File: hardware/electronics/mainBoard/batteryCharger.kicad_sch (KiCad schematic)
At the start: 48 parts, among them J11 M8AS-02PFFR-SF8001, J8 S2B-PH-SM4-TB, Q1 CSD17575Q3, Q6 VAL, Q7 VAL, Q8 VAL, Q9 VAL, U11 BQ25798

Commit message: added jumpers
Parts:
- added JP1: ~, symbol .DS-Jumpers:Jumper_2_Bridged
- R60: value 6K04 -> 8K2; DKPN 541-6.04KLCT-ND -> (none); MPN CRCW04026K04FKED -> (none)
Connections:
- net at D11.2: now also JP1.1; no longer U11.1 (STAT)
- new net: JP1.2, U11.1 (STAT)
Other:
- moved on the sheet: D11, R59
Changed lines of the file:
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@@
 	(title_block
 		(title "Battery Charger")
-		(date "2025-02-26")
+		(date "2025-03-03")
 		(rev "1")
 		(comment 2 "PROTOTYPE")
@@
 	(wire
 		(pts
-			(xy 144.78 123.19) (xy 161.29 123.19)
+			(xy 144.78 123.19) (xy 160.02 123.19)
 		)
 		(stroke
@@
 	(wire
 		(pts
-			(xy 85.09 137.16) (xy 88.9 137.16)
+			(xy 74.93 137.16) (xy 78.74 137.16)
 		)
 		(stroke
@@
 	(wire
 		(pts
-			(xy 74.93 137.16) (xy 80.01 137.16)
+			(xy 64.77 137.16) (xy 69.85 137.16)
 		)
 		(stroke
@@
 	(wire
 		(pts
-			(xy 161.29 120.65) (xy 161.29 123.19)
+			(xy 160.02 120.65) (xy 160.02 123.19)
 		)
 		(stroke
@@
 	(wire
 		(pts
+			(xy 83.82 137.16) (xy 88.9 137.16)
+		)
+		(stroke
+			(width 0)
+			(type default)
+		)
+	)
+	(wire
+		(pts
 			(xy 62.23 53.34) (xy 69.85 53.34)
 		)
@@
 	(wire
 		(pts
+			(xy 93.98 137.16) (xy 96.52 137.16)
+		)
+		(stroke
+			(width 0)
+			(type default)
+		)
+	)
+	(wire
+		(pts
 			(xy 77.47 53.34) (xy 77.47 58.42)
 		)
@@
 	(wire
 		(pts
-			(xy 93.98 137.16) (xy 96.52 137.16)
-		)
-		(stroke
-			(width 0)
-			(type default)
-		)
-	)
-	(wire
-		(pts
 			(xy 45.72 53.34) (xy 45.72 54.61)
 		)
@@
 		)
 	)
+	(label "~{QON}"
+		(at 92.71 152.4 0)
+		(effects
+			(font
+				(size 1.27 1.27)
+			)
+			(justify left bottom)
+		)
+	)
 	(label "TS"
 		(at 129.54 128.27 180)
@@
 		)
 	)
+	(label "TS"
+		(at 227.33 105.41 0)
+		(effects
+			(font
+				(size 1.27 1.27)
+			)
+			(justify left bottom)
+		)
+	)
 	(label "REGN"
-		(at 74.93 137.16 0)
+		(at 64.77 137.16 0)
 		(effects
 			(font
@@
 		)
 	)
+	(label "~{CE}"
+		(at 92.71 142.24 0)
+		(effects
+			(font
+				(size 1.27 1.27)
+			)
+			(justify left bottom)
+		)
+	)
 	(label "PMID"
 		(at 132.08 85.09 180)
@@
 		)
 	)
+	(label "BAT_CHG_INT"
+		(at 83.82 149.86 0)
+		(effects
+			(font
+				(size 1.27 1.27)
+			)
+			(justify left bottom)
+		)
+	)
 	(label "REGN"
 		(at 213.36 90.17 270)
@@
 	)
 	(symbol
+		(lib_id ".DS-Jumpers:Jumper_2_Bridged")
+		(at 91.44 137.16 0)
+		(unit 1)
+		(exclude_from_sim no)
+		(in_bom no)
+		(on_board yes)
+		(dnp no)
+		(fields_autoplaced yes)
+		(property "Reference" "JP1"
+			(at 91.44 135.255 0)
+			(do_not_autoplace yes)
+			(effects
+				(font
+					(size 1.27 1.27)
+				)
+			)
+		)
+		(property "Value" "~"
+			(at 91.44 134.62 0)
+			(effects
+				(font
+					(size 1.27 1.27)
+				)
+			)
+		)
+		(property "Footprint" ""
+			(at 91.44 137.16 0)
+			(effects
+				(font
+					(size 1.27 1.27)
+				)
+				(hide yes)
+			)
+		)
+		(property "Datasheet" ""
+			(at 91.44 137.16 0)
+			(effects
+				(font
+					(size 1.27 1.27)
+				)
+				(hide yes)
+			)
+		)
+		(property "Description" ""
+			(at 91.44 137.16 0)
+			(effects
+				(font
+					(size 1.27 1.27)
+				)
+				(hide yes)
+			)
+		)
+		(pin "1"
+		)
+		(pin "2"
+		)
+		(instances
+			(project ""
+				(path "/be16e32f-2ccf-4272-9ec7-94d5fe7a55e0/358f4008-8d95-4575-a32e-016ac6c7f14c/e4a7374c-b8e2-4805-9d19-02e8c1eab01e"
+					(reference "JP1")
+					(unit 1)
+				)
+			)
+		)
+	)
+	(symbol
 		(lib_id "lib_sch:GND")
 		(at 85.09 74.93 0)
@@
 		(on_board yes)
 		(dnp no)
-		(fields_autoplaced yes)
 		(property "Reference" "#PWR0151"
 			(at 86.36 132.08 0)
@@
 	(symbol
 		(lib_id "lib_sch:R_horizontal")
-		(at 82.55 137.16 0)
+		(at 72.39 137.16 0)
 		(unit 1)
 		(exclude_from_sim no)
@@
 		(fields_autoplaced yes)
 		(property "Reference" "R59"
-			(at 82.55 135.89 0)
+			(at 72.39 135.89 0)
 			(do_not_autoplace yes)
 			(effects
@@
 		)
 		(property "Value" "2K2"
-			(at 82.55 138.43 0)
+			(at 72.39 138.43 0)
 			(do_not_autoplace yes)
 			(effects
@@
 		)
 		(property "Footprint" "lib_fp:CRCW0402"
-			(at 80.01 137.16 90)
+			(at 69.85 137.16 90)
 			(effects
 				(font
@@
 		)
 		(property "Datasheet" "datasheets/Vishay-Dale-DRCWe3.pdf"
-			(at 80.01 137.16 90)
+			(at 69.85 137.16 90)
 			(effects
 				(font
@@
 		)
 		(property "Description" "RES SMD 2.2K OHM 1% 1/16W 0402"
-			(at 82.55 137.16 0)
+			(at 72.39 137.16 0)
 			(effects
 				(font
@@
 		)
 		(property "Manufacturer" "Vishay Dale"
-			(at 80.01 137.16 90)
+			(at 69.85 137.16 90)
 			(effects
 				(font
@@
 		)
 		(property "MPN" "CRCW04022K20FKED"
-			(at 80.01 137.16 90)
+			(at 69.85 137.16 90)
 			(effects
 				(font
@@
 		)
 		(property "DKPN" "541-2.20KLCT-ND"
-			(at 82.55 137.16 0)
+			(at 72.39 137.16 0)
 			(effects
 				(font
@@
 		)
 		(property "Tolerance" "1%"
-			(at 82.55 139.7 0)
+			(at 72.39 139.7 0)
 			(do_not_autoplace yes)
 			(effects
@@
 		)
 		(property "Power Rating" "62.5mW"
-			(at 82.55 138.43 0)
+			(at 72.39 138.43 0)
 			(do_not_autoplace yes)
 			(effects
@@
 		)
 		(property "Package" "0402"
-			(at 82.55 139.7 0)
+			(at 72.39 139.7 0)
 			(do_not_autoplace yes)
 			(effects
@@
 		)
 		(property "Zener Voltage" ""
-			(at 82.55 137.16 0)
+			(at 72.39 137.16 0)
 			(effects
 				(font
@@
 			)
 		)
-		(property "Value" "6K04"
+		(property "Value" "8K2"
 			(at 132.08 93.98 0)
 			(do_not_autoplace yes)
@@
 			)
 		)
-		(property "Description" "RES SMD 6.04K OHM 1% 1/16W 0402"
+		(property "Description" ""
 			(at 132.08 92.71 0)
 			(effects
@@
 			)
 		)
-		(property "MPN" "CRCW04026K04FKED"
+		(property "MPN" ""
 			(at 129.54 92.71 90)
 			(effects
@@
 			)
 		)
-		(property "DKPN" "541-6.04KLCT-ND"
+		(property "DKPN" ""
 			(at 132.08 92.71 0)
 			(effects
@@
 			)
 		)
-		(property "Zener Voltage" ""
-			(at 132.08 92.71 0)
-			(effects
-				(font
-					(size 1.27 1.27)
-				)
-				(hide yes)
-			)
-		)
 		(pin "1"
 		)
@@
 	(symbol
 		(lib_id "lib_sch:LED_horizontal")
-		(at 91.44 137.16 0)
+		(at 81.28 137.16 0)
 		(unit 1)
 		(exclude_from_sim no)
@@
 		(fields_autoplaced yes)
 		(property "Reference" "D11"
-			(at 91.44 135.636 0)
+			(at 81.28 135.636 0)
 			(do_not_autoplace yes)
 			(effects
@@
 		)
 		(property "Value" "LTST-C171GKT"
-			(at 91.44 138.684 0)
+			(at 81.28 138.684 0)
 			(do_not_autoplace yes)
 			(effects
@@
 		)
 		(property "Footprint" "lib_fp:LTST-0805"
-			(at 91.44 137.16 0)
+			(at 81.28 137.16 0)
 			(effects
 				(font
@@
 		)
 		(property "Datasheet" "datasheets/Lite-On-LTST-C171GKT.pdf"
-			(at 91.44 137.16 0)
+			(at 81.28 137.16 0)
 			(effects
 				(font
@@
 		)
 		(property "Description" "LED GREEN CLEAR CHIP SMD"
-			(at 91.44 137.16 0)
+			(at 81.28 137.16 0)
 			(effects
 				(font
@@
 		)
 		(property "Manufacturer" "Lite-On Inc."
-			(at 91.44 137.16 0)
+			(at 81.28 137.16 0)
 			(effects
 				(font
@@
 		)
 		(property "MPN" "LTST-C171GKT"
-			(at 91.44 137.16 0)
+			(at 81.28 137.16 0)
 			(effects
 				(font
@@
 		)
 		(property "DKPN" "160-1423-1-ND"
-			(at 91.44 137.16 0)
+			(at 81.28 137.16 0)
 			(effects
 				(font
@@
 		)
 		(property "Forward Voltage" "2V1"
-			(at 91.44 139.954 0)
+			(at 81.28 139.954 0)
 			(do_not_autoplace yes)
 			(effects
@@
 		)
 		(property "Current" "20mA"
-			(at 91.44 139.954 0)
+			(at 81.28 139.954 0)
 			(do_not_autoplace yes)
 			(effects
@@
 		)
 		(property "Zener Voltage" ""
-			(at 91.44 137.16 0)
+			(at 81.28 137.16 0)
 			(effects
 				(font
@@
 	(symbol
 		(lib_id "lib_sch:CHG+")
-		(at 161.29 120.65 0)
+		(at 160.02 120.65 0)
 		(unit 1)
 		(exclude_from_sim no)
@@
 		(fields_autoplaced yes)
 		(property "Reference" "#PWR0178"
-			(at 161.29 120.65 0)
+			(at 160.02 120.65 0)
 			(effects
 				(font
@@
 		)
 		(property "Value" "CHG+"
-			(at 161.29 117.094 0)
+			(at 160.02 117.094 0)
 			(do_not_autoplace yes)
 			(effects
@@
 		)
 		(property "Footprint" ""
-			(at 161.29 120.65 0)
+			(at 160.02 120.65 0)
 			(effects
 				(font
@@
 		)
 		(property "Datasheet" ""
-			(at 161.29 120.65 0)
+			(at 160.02 120.65 0)
 			(effects
 				(font
@@
 		)
 		(property "Description" ""
-			(at 161.29 120.65 0)
+			(at 160.02 120.65 0)
 			(effects
 				(font

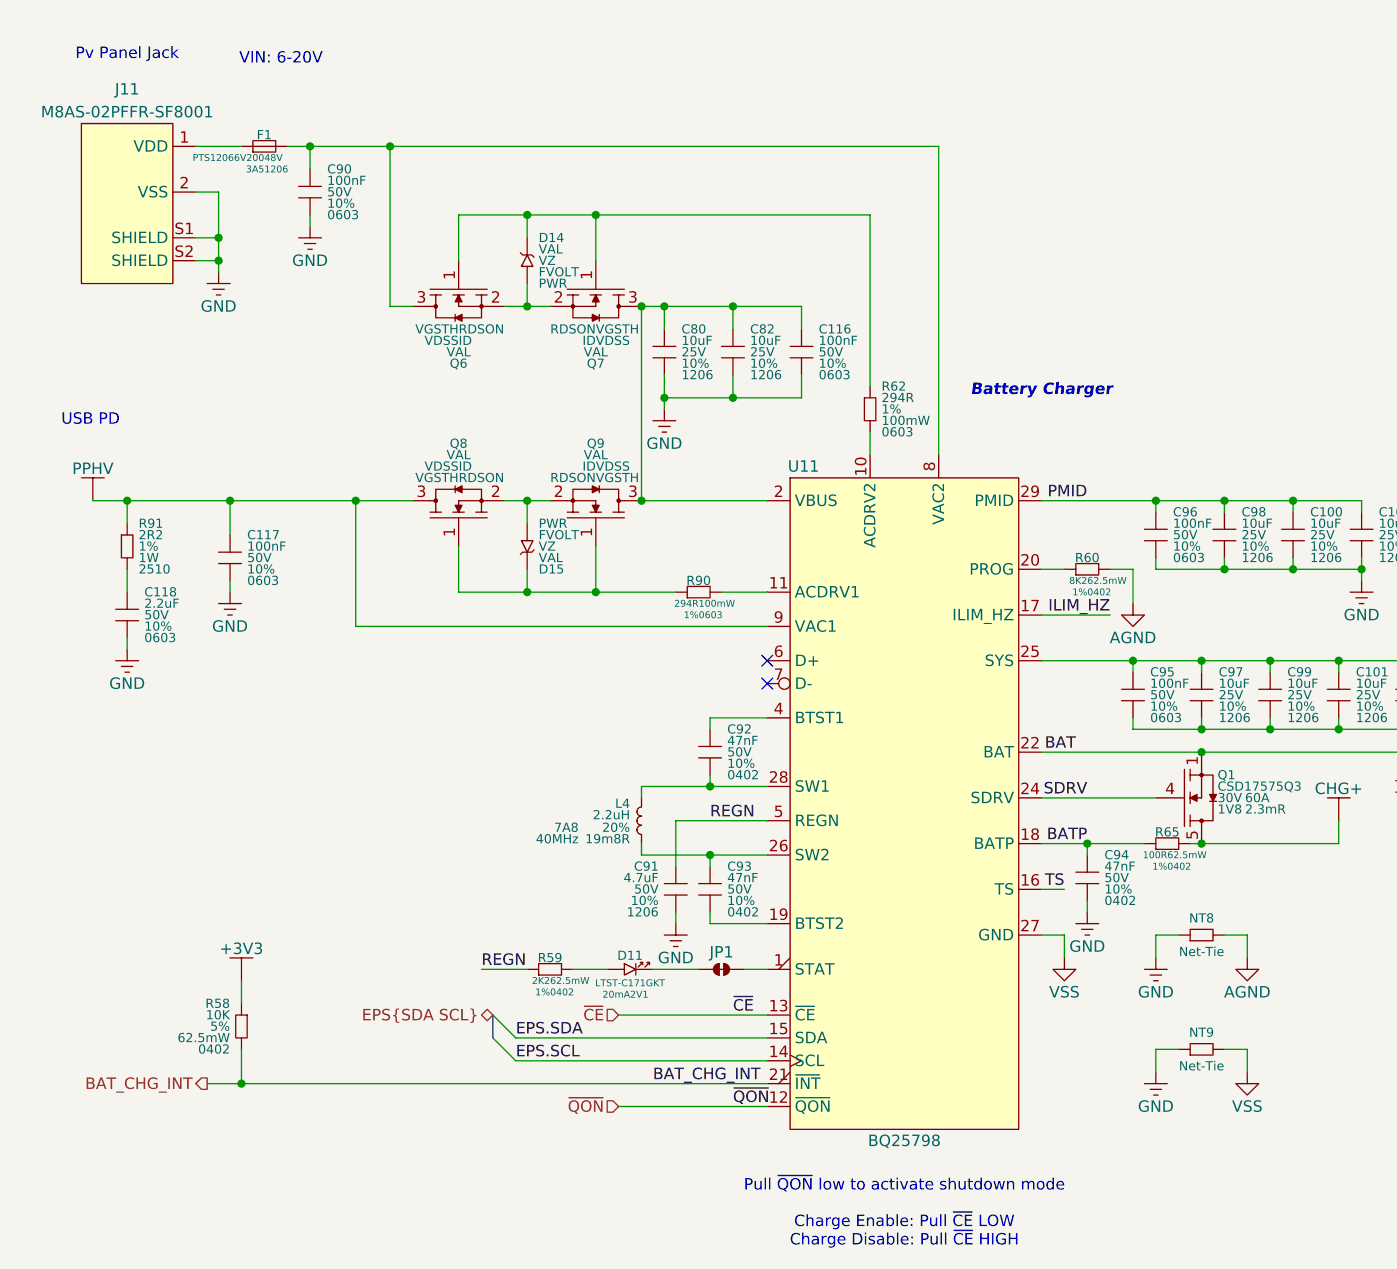
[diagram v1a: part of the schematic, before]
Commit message: heiarchical sheet pins
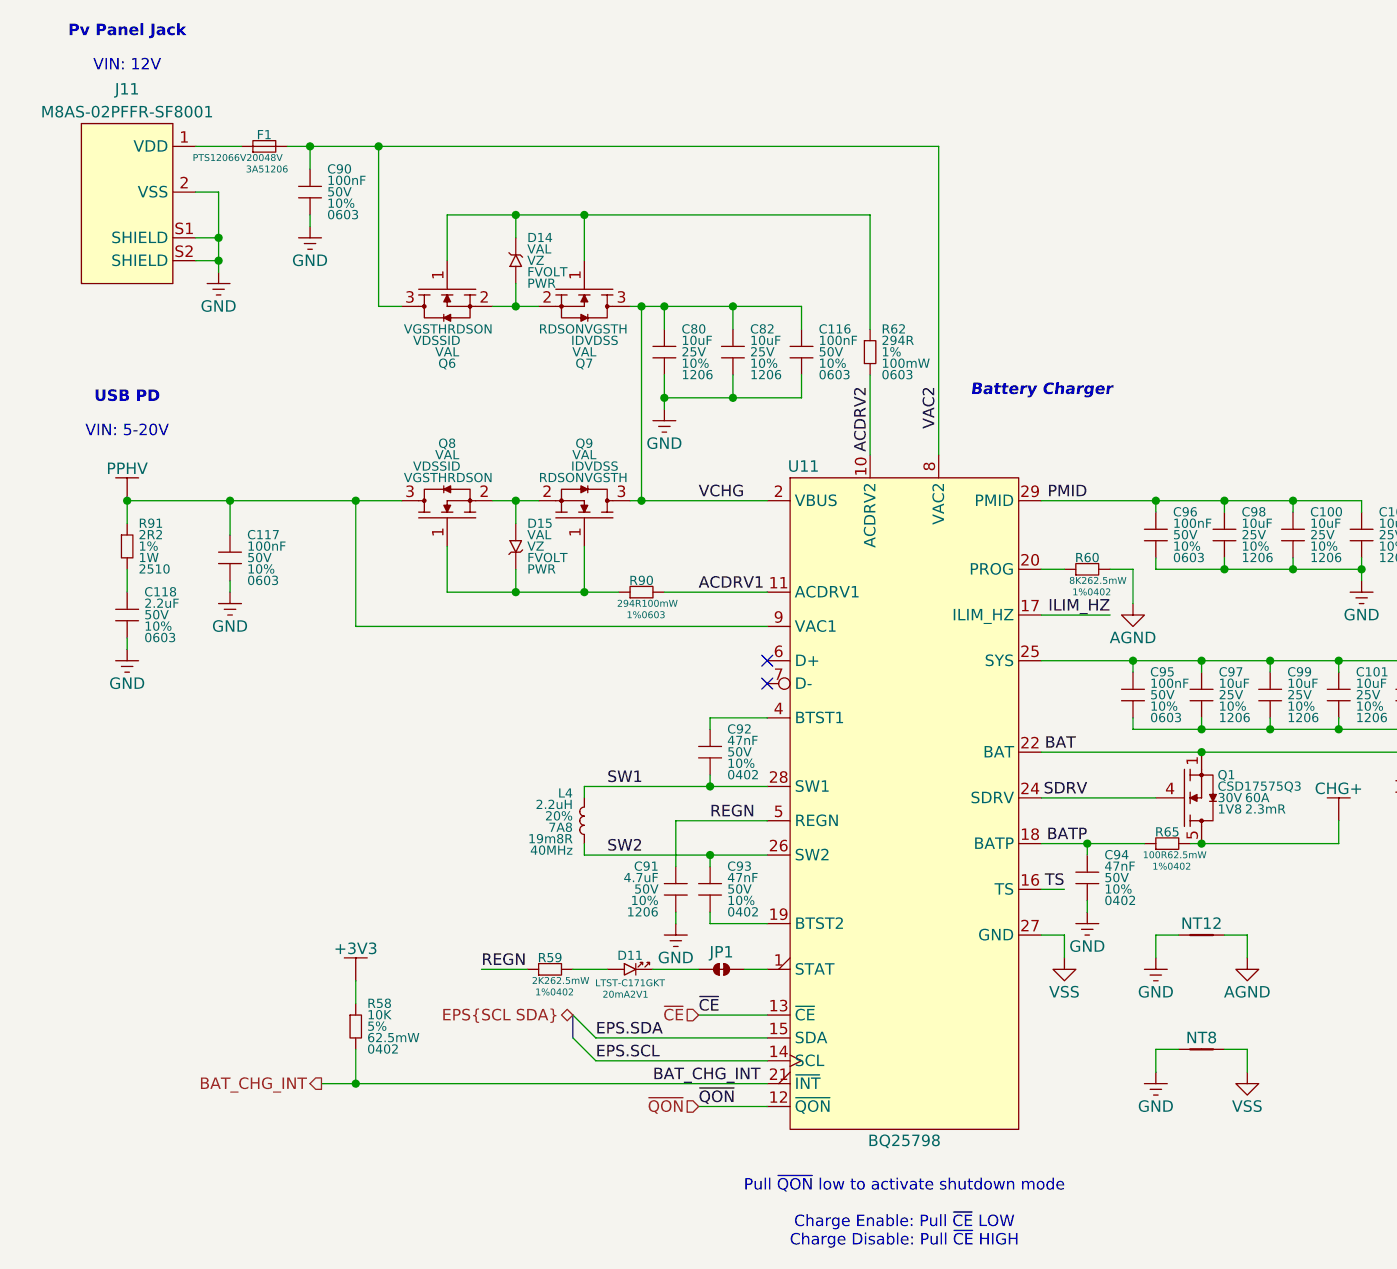
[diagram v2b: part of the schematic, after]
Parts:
- removed NT8, NT9: Net-Tie, lib_fp:NetTie-2_SMD_Pad2.0mm, symbol lib_sch:NT
- added NT12, NT8: NetTie_2, symbol lib_sch:NetTie_2
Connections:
- net AGND: now also NT12.2
- net GND: now also NT12.1, NT8.1
- net VSS: now also NT8.2
- net ACDRV1: now reaches R90.2, U11.11 (ACDRV1)
- net VAC2: now reaches C90.1, F1.2, Q6.3, U11.8 (VAC2)
- net ACDRV2: now reaches R62.2, U11.10 (ACDRV2)
- net SW2: now reaches C93.1, L4.2, U11.26 (SW2)
- net SW1: now reaches C92.2, L4.1, U11.28 (SW1)
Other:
- note added: "VIN: 12V"
- note added: "VIN: 5-20V"
- note removed: "VIN: 6-20V"
- moved on the sheet: D14, D15, L4, Q6, Q7, Q8, Q9, R58, R62, R90

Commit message: fixed schematic
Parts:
- removed C117, C90, C95, C96: 100nF, lib_fp:MLCC0603, symbol lib_sch:C
- removed R58: 10K, lib_fp:CRCW0402, symbol lib_sch:R
- removed R65: 100R, lib_fp:CRCW0402, symbol lib_sch:R_horizontal
- added C106, C109, C110, C114: 100nF, symbol lib_sch:C
- added R70: 100R, symbol lib_sch:R_horizontal
- added R72: 10K, symbol lib_sch:R
- C107: renamed from C80; footprint lib_fp:MLCC1206 -> (none); DKPN 445-CGA5L1X7R1E106K160DCCT-ND -> 490-4798-1-ND; MPN CGA5L1X7R1E106K160DC -> GCM32ER71E106KA57L; Manufacturer TDK Corporation -> Murata Electronics; Package 1206 -> 1210
- C108: renamed from C82; footprint lib_fp:MLCC1206 -> (none); DKPN 445-CGA5L1X7R1E106K160DCCT-ND -> 490-4798-1-ND; MPN CGA5L1X7R1E106K160DC -> GCM32ER71E106KA57L; Manufacturer TDK Corporation -> Murata Electronics; Package 1206 -> 1210
- C111: renamed from C98; footprint lib_fp:MLCC1206 -> (none); DKPN 445-CGA5L1X7R1E106K160DCCT-ND -> 490-4798-1-ND; MPN CGA5L1X7R1E106K160DC -> GCM32ER71E106KA57L; Manufacturer TDK Corporation -> Murata Electronics; Package 1206 -> 1210
- C112: renamed from C100; footprint lib_fp:MLCC1206 -> (none); DKPN 445-CGA5L1X7R1E106K160DCCT-ND -> 490-4798-1-ND; MPN CGA5L1X7R1E106K160DC -> GCM32ER71E106KA57L; Manufacturer TDK Corporation -> Murata Electronics; Package 1206 -> 1210
- C113: renamed from C102; footprint lib_fp:MLCC1206 -> (none); DKPN 445-CGA5L1X7R1E106K160DCCT-ND -> 490-4798-1-ND; MPN CGA5L1X7R1E106K160DC -> GCM32ER71E106KA57L; Manufacturer TDK Corporation -> Murata Electronics; Package 1206 -> 1210
- C115: renamed from C118; footprint lib_fp:MLCC0603 -> (none); DKPN 478-KAM15AR71H104KMCT-ND -> 478-KAF31GR71H225KUCT-ND; MPN KAM15AR71H104KM -> KAF31GR71H225KU; Package 0603 -> 1206
- C116: footprint lib_fp:MLCC0603 -> (none); DKPN 478-KAM15AR71H104KMCT-ND -> 478-KAM15AR71H104KTCT-ND; MPN KAM15AR71H104KM -> 06035C104K4T2A
- C117: renamed from C97; footprint lib_fp:MLCC1206 -> (none); DKPN 445-CGA5L1X7R1E106K160DCCT-ND -> 490-4798-1-ND; MPN CGA5L1X7R1E106K160DC -> GCM32ER71E106KA57L; Manufacturer TDK Corporation -> Murata Electronics; Package 1206 -> 1210
- C118: renamed from C99; footprint lib_fp:MLCC1206 -> (none); DKPN 445-CGA5L1X7R1E106K160DCCT-ND -> 490-4798-1-ND; MPN CGA5L1X7R1E106K160DC -> GCM32ER71E106KA57L; Manufacturer TDK Corporation -> Murata Electronics; Package 1206 -> 1210
- C119: renamed from C101; footprint lib_fp:MLCC1206 -> (none); DKPN 445-CGA5L1X7R1E106K160DCCT-ND -> 490-4798-1-ND; MPN CGA5L1X7R1E106K160DC -> GCM32ER71E106KA57L; Manufacturer TDK Corporation -> Murata Electronics; Package 1206 -> 1210
- C120: renamed from C103; footprint lib_fp:MLCC1206 -> (none); DKPN 445-CGA5L1X7R1E106K160DCCT-ND -> 490-4798-1-ND; MPN CGA5L1X7R1E106K160DC -> GCM32ER71E106KA57L; Manufacturer TDK Corporation -> Murata Electronics; Package 1206 -> 1210
- C121: renamed from C105; footprint lib_fp:MLCC1206 -> (none); DKPN 445-CGA5L1X7R1E106K160DCCT-ND -> 490-4798-1-ND; MPN CGA5L1X7R1E106K160DC -> GCM32ER71E106KA57L; Manufacturer TDK Corporation -> Murata Electronics; Package 1206 -> 1210
- C122: renamed from C92; footprint lib_fp:MLCC0402 -> (none); DKPN 478-KAM05AR71H472KHCT-ND -> 478-KAM15AR71H472JTCT-ND; MPN 04025C472K4T2A -> 06035C472J4T2A; Package 0402 -> 0603; Tolerance 10% -> 5%
- C123: renamed from C104; footprint lib_fp:MLCC1206 -> (none); DKPN 445-CGA5L1X7R1E106K160DCCT-ND -> 490-4798-1-ND; MPN CGA5L1X7R1E106K160DC -> GCM32ER71E106KA57L; Manufacturer TDK Corporation -> Murata Electronics; Package 1206 -> 1210
- C124: renamed from C106; footprint lib_fp:MLCC1206 -> (none); DKPN 445-CGA5L1X7R1E106K160DCCT-ND -> 490-4798-1-ND; MPN CGA5L1X7R1E106K160DC -> GCM32ER71E106KA57L; Manufacturer TDK Corporation -> Murata Electronics; Package 1206 -> 1210
- C125: renamed from C94; footprint lib_fp:MLCC0402 -> (none); DKPN 478-KAM05AR71H472KHCT-ND -> 478-KAM15AR71H472JTCT-ND; MPN 04025C472K4T2A -> 06035C472J4T2A; Package 0402 -> 0603; Tolerance 10% -> 5%
- C126: renamed from C91; footprint lib_fp:MLCC1206 -> (none)
- C127: renamed from C93; footprint lib_fp:MLCC0402 -> (none); DKPN 478-KAM05AR71H472KHCT-ND -> 478-KAM15AR71H472JTCT-ND; MPN 04025C472K4T2A -> 06035C472J4T2A; Package 0402 -> 0603; Tolerance 10% -> 5%
- D14, D15: value VAL -> BZT52C12T-7; DKPN (none) -> BZT52C12T-7DICT-ND; Forward Voltage FVOLT -> 900mV; MPN (none) -> BZT52C12T-7; Manufacturer (none) -> Diodes Incorporated; Power Rating PWR -> 300mW; Zener Voltage VZ -> 12V
- D16: renamed from D11; value LTST-C171GKT -> LTST-C191KGKT; footprint lib_fp:LTST-0805 -> (none); Color (none) -> GREEN; DKPN 160-1423-1-ND -> 160-1446-1-ND; Forward Voltage 2V1 -> 2V; MPN LTST-C171GKT -> LTST-C191KGKT
- F1: value PTS12066V200 -> 2920L500/24SLDR; footprint lib_fp:PTS1206 -> (none); DKPN 283-PTS12066V200CT-ND -> 18-2920L500/24SLDRCT-ND; MPN PTS12066V200 -> 2920L500/24SLDR; Manufacturer Eaton - Electronics Division -> Littelfuse Inc.; Package 1206 -> 2920; Trip Current 3A5 -> 10A; Voltage 48V -> 24V
- J18: renamed from J11; DKPN (none) -> M8AS-02PFFR-SF8001-ND; MPN (none) -> M8AS-02PFFR-SF8001; Manufacturer (none) -> Amphenol LTW
- J19: renamed from J8; footprint lib_fp:JST-PH-S2B-SM4-TB -> (none)
- JP10: renamed from JP1; symbol .DS-Jumpers:Jumper_2_Bridged -> lib_sch:Jumper_2_Bridged
- L6: renamed from L4; footprint lib_fp:WE-XHMI-4030 -> (none); DC Resistance 19m8R -> 16m6R
- Q1: renamed from Q6; value VAL -> CSD17581Q3A; DKPN (none) -> 296-47754-1-ND; ID ID -> 21A; MPN (none) -> CSD17581Q3A; Manufacturer (none) -> Texas Instruments; RDSON RDSON -> 3m8R; VDSS VDSS -> 30V; VGSTH VGSTH -> 1V7
- Q2: renamed from Q7; value VAL -> CSD17581Q3A; DKPN (none) -> 296-47754-1-ND; ID ID -> 21A; MPN (none) -> CSD17581Q3A; Manufacturer (none) -> Texas Instruments; RDSON RDSON -> 3m8R; VDSS VDSS -> 30V; VGSTH VGSTH -> 1V7
- Q3: renamed from Q8; value VAL -> CSD17581Q3A; DKPN (none) -> 296-47754-1-ND; ID ID -> 21A; MPN (none) -> CSD17581Q3A; Manufacturer (none) -> Texas Instruments; RDSON RDSON -> 3m8R; VDSS VDSS -> 30V; VGSTH VGSTH -> 1V7
- Q4: renamed from Q9; value VAL -> CSD17581Q3A; DKPN (none) -> 296-47754-1-ND; ID ID -> 21A; MPN (none) -> CSD17581Q3A; Manufacturer (none) -> Texas Instruments; RDSON RDSON -> 3m8R; VDSS VDSS -> 30V; VGSTH VGSTH -> 1V7
- Q5: renamed from Q1; footprint lib_fp:SON8P65_330X330X100L45X34N -> (none); DKPN 296-39994-1-ND -> 296-35628-1-ND; ID 60A -> 100A; MPN CSD17575Q3 -> CSD18532Q5B; RDSON 2.3mR -> 3.2mR; VDSS 30V -> 60V; VGSTH 1V8 -> 2V2
- R66: renamed from R62; footprint lib_fp:CRCW0402 -> (none); DKPN 541-10KJCT-ND -> 541-294LCT-ND; MPN CRCW040210K0JNED -> CRCW0402294RFKED; Package 0603 -> 0402; Power Rating 100mW -> 62m5W
- R67: renamed from R91; footprint lib_fp:CRCW0402 -> (none); DKPN 541-10KJCT-ND -> 541-CRCW25122R20FKEGCT-ND; MPN CRCW040210K0JNED -> CRCW25122R20FKEG; Package 2510 -> 2512
- R68: renamed from R60; footprint lib_fp:CRCW0402 -> (none); DKPN (none) -> 541-8.20KLCT-ND; MPN (none) -> CRCW04028K20FKED; Power Rating 62.5mW -> 62m5W
- R69: renamed from R90; footprint lib_fp:CRCW0402 -> (none); Package 0603 -> 0402; Power Rating 100mW -> 62m5W
- R71: renamed from R59; footprint lib_fp:CRCW0402 -> (none); Power Rating 62.5mW -> 62m5W
- R73: renamed from R66; footprint lib_fp:CRCW0402 -> (none); Power Rating 62.5mW -> 62m5W
- R74: renamed from R68; footprint lib_fp:CRCW0402 -> (none); Power Rating 62.5mW -> 62m5W
- R75: renamed from R67; footprint lib_fp:CRCW0402 -> (none); Power Rating 62.5mW -> 62m5W
- R76: renamed from R69; footprint lib_fp:CRCW0402 -> (none); Power Rating 62.5mW -> 62m5W
- U22: renamed from U11; footprint lib_fp:RQM0029A -> (none)
- renumbered NT12 to NT8, NT8 to NT9
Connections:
- net +3V3: now also R72.1
- net BATP: now also Q5.5, Q5.6, Q5.7, Q5.8, R70.1
- net BAT_CHG_INT: now also R72.2
- net CHG+: now also R70.2; no longer Q5.5, Q5.6, Q5.7, Q5.8
- net GND: now also C106.2, C109.2, C110.2, C114.2
- net PMID: now also C110.1
- net PPHV: now also C114.1
- net VAC2: now also C106.1
- net VSYS: now also C116.1
- net PROG: now reaches R68.1, U22.20 (PROG)
- net BTST2: now reaches C127.2, U22.19 (BTST2)
- net VBUS renamed VCHG
- net VCHG: now also C109.1; no longer C116.1
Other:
- note added: "I2C Address: 0x6B"
- moved on the sheet: C107, C108, C111, C112, C113, C115, C117, C118, C119, C120, C121, C122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
